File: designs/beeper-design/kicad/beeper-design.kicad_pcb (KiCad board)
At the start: 4 copper layers, 27.5 x 19 mm, 104 parts

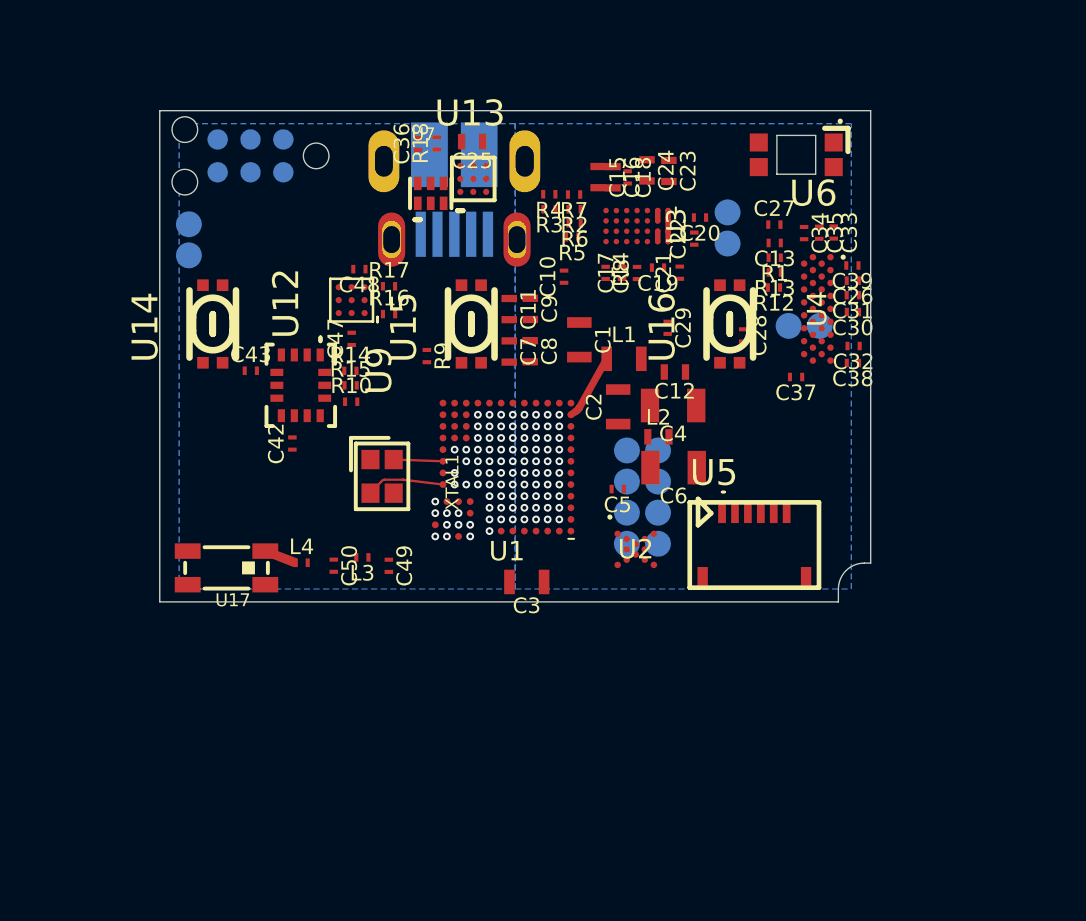
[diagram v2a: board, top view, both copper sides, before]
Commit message: better export + JLCPCB numbers
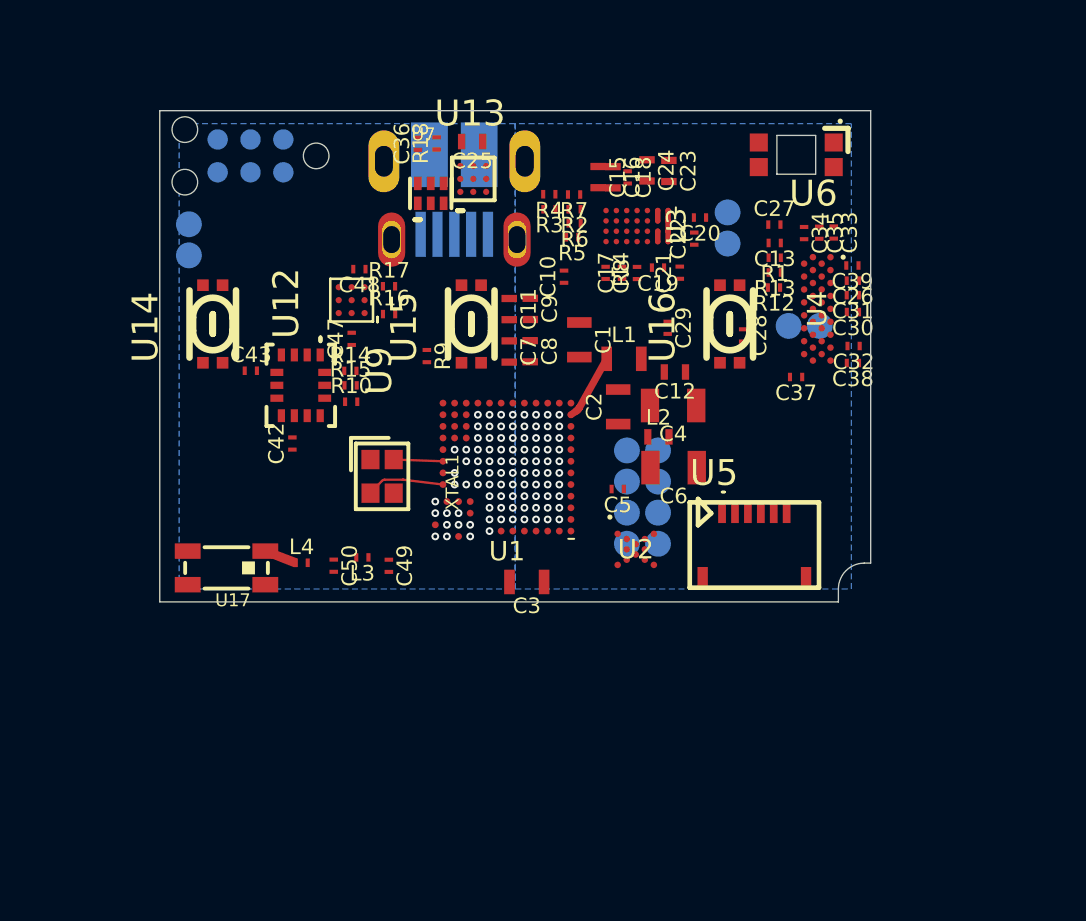
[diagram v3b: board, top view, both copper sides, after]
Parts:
- C10: footprint beeper-design:Pkg0201_18 -> beeper-design:Pkg0201_11
- C11: footprint beeper-design:Pkg0402_6 -> beeper-design:Pkg0402_1
- C12: footprint beeper-design:Pkg0402_5 -> beeper-design:Pkg0402
- C13: footprint beeper-design:Pkg0201_34 -> beeper-design:Pkg0201_27
- C14: footprint beeper-design:Pkg0201_2 -> beeper-design:Pkg0201_41
- C15: footprint beeper-design:Pkg0402_10 -> beeper-design:Pkg0402_5
- C16: footprint beeper-design:Pkg0402_4 -> beeper-design:Pkg0402_10
- C17: footprint beeper-design:Pkg0201_21 -> beeper-design:Pkg0201_14
- C18: footprint beeper-design:Pkg0201_33 -> beeper-design:Pkg0201_26
- C19: footprint beeper-design:Pkg0201_43 -> beeper-design:Pkg0201_36
- C20: footprint beeper-design:Pkg0201_6 -> beeper-design:Pkg0201_45
- C21: footprint beeper-design:Pkg0201_19 -> beeper-design:Pkg0201_12
- C22: footprint beeper-design:Pkg0201_30 -> beeper-design:Pkg0201_23
- C23: footprint beeper-design:Pkg0402_8 -> beeper-design:Pkg0402_3
- C24: footprint beeper-design:Pkg0402_2 -> beeper-design:Pkg0402_8
- C25: footprint beeper-design:Pkg0402 -> beeper-design:Pkg0402_6
- C26: footprint beeper-design:Pkg0201_44 -> beeper-design:Pkg0201_37
- C27: footprint beeper-design:Pkg0201_5 -> beeper-design:Pkg0201_44
- C28: footprint beeper-design:Pkg0201_17 -> beeper-design:Pkg0201_10
- C29: footprint beeper-design:Pkg0201_29 -> beeper-design:Pkg0201_22
- C30: footprint beeper-design:Pkg0201_15 -> beeper-design:Pkg0201_8
- C31: footprint beeper-design:Pkg0201_28 -> beeper-design:Pkg0201_21
- C32: footprint beeper-design:Pkg0201_40 -> beeper-design:Pkg0201_33
- C33: footprint beeper-design:Pkg0201_3 -> beeper-design:Pkg0201_42
- C34: footprint beeper-design:Pkg0201_14 -> beeper-design:Pkg0201_7
- C35: footprint beeper-design:Pkg0201_38 -> beeper-design:Pkg0201_31
- C36: footprint beeper-design:Pkg0201_31 -> beeper-design:Pkg0201_24
- C37: footprint beeper-design:Pkg0201_42 -> beeper-design:Pkg0201_35
- C38: footprint beeper-design:Pkg0201_4 -> beeper-design:Pkg0201_43
- C39: footprint beeper-design:Pkg0201_26 -> beeper-design:Pkg0201_19
- C42: footprint beeper-design:Pkg0201_45 -> beeper-design:Pkg0201_38
- C43: footprint beeper-design:Pkg0201_8 -> beeper-design:Pkg0201_1
- C47: footprint beeper-design:Pkg0201_10 -> beeper-design:Pkg0201_3
- C48: footprint beeper-design:Pkg0201_22 -> beeper-design:Pkg0201_15
- C49: footprint beeper-design:Pkg0201_39 -> beeper-design:Pkg0201_32
- C5: footprint beeper-design:Pkg0201_7 -> beeper-design:Pkg0201
- C50: footprint beeper-design:Pkg0201_9 -> beeper-design:Pkg0201_2
- C7: footprint beeper-design:Pkg0402_7 -> beeper-design:Pkg0402_2
- C8: footprint beeper-design:Pkg0402_9 -> beeper-design:Pkg0402_4
- C9: footprint beeper-design:Pkg0402_3 -> beeper-design:Pkg0402_9
- J1: value ~ -> TC2030-IDC-NL
- J6: value ~ -> 10103594-0001LF
- L2: footprint beeper-design:Pkg0402_1 -> beeper-design:Pkg0402_7
- L3: footprint beeper-design:Pkg0201_1 -> beeper-design:Pkg0201_40
- L4: footprint beeper-design:Pkg0201_16 -> beeper-design:Pkg0201_9
- R1: footprint beeper-design:Pkg0201_25 -> beeper-design:Pkg0201_18
- R10: footprint beeper-design:Pkg0201_41 -> beeper-design:Pkg0201_34
- R12, R13: footprint beeper-design:Pkg0201_27 -> beeper-design:Pkg0201_20
- R14, R15: footprint beeper-design:Pkg0201_12 -> beeper-design:Pkg0201_5
- R16, R17: footprint beeper-design:Pkg0201_37 -> beeper-design:Pkg0201_30
- R18: footprint beeper-design:Pkg0201_20 -> beeper-design:Pkg0201_13
- R2: footprint beeper-design:Pkg0201_13 -> beeper-design:Pkg0201_6
- R3: footprint beeper-design:Pkg0201_24 -> beeper-design:Pkg0201_17
- R4: footprint beeper-design:Pkg0201_36 -> beeper-design:Pkg0201_29
- R5: footprint beeper-design:Pkg0201 -> beeper-design:Pkg0201_39
- R6: footprint beeper-design:Pkg0201_11 -> beeper-design:Pkg0201_4
- R7: footprint beeper-design:Pkg0201_23 -> beeper-design:Pkg0201_16
- R8: footprint beeper-design:Pkg0201_35 -> beeper-design:Pkg0201_28
- R9: footprint beeper-design:Pkg0201_32 -> beeper-design:Pkg0201_25
- U1: value ~ -> DA14705-00000HZ2; footprint beeper-design:LP_1 -> beeper-design:LP
- U12: value ~ -> DRV2605YZFR; footprint beeper-design:LP -> beeper-design:LP_8
- U13: value ~ -> CSD75207W15; footprint beeper-design:LP_7 -> beeper-design:LP_6
- U14, U15, U16: value ~ -> EVPBB4A9B000; footprint beeper-design:LP_3 -> beeper-design:LP_2
- U2: value ~ -> AT25FF321A-UUN-T
- U3: value ~ -> BQ51003YFPR; footprint beeper-design:LP_8 -> beeper-design:LP_7
- U4: value ~ -> DA7212-01UM2; footprint beeper-design:LP_4 -> beeper-design:LP_3
- U5: value ~ -> FH19C-6S-0.5SH(10); footprint beeper-design:LP_6 -> beeper-design:LP_5
- U6: value ~ -> 23-23B/R6GHBHW-C30/2A; footprint beeper-design:LP_5 -> beeper-design:LP_4
- U7: value ~ -> TPD4S012DRYR
- U9: value ~ -> LSM6DSOXTR; footprint beeper-design:LP_2 -> beeper-design:LP_1
- XTAL1: value ~ -> XRCGB32M000F1H00R0
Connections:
- net AC1 renamed Net-(C15-Pad1)
- net AC2 renamed Net-(C16-Pad1)
- net AD renamed Net-(U3-AD)
- net BOOT1 renamed Net-(U3-BOOT1)
- net BOOT2 renamed Net-(U3-BOOT2)
- net CLAMP1 renamed Net-(U3-CLAMP1)
- net CLAMP2 renamed Net-(U3-CLAMP2)
- net COMM1 renamed Net-(U3-COMM1)
- net COMM2 renamed Net-(U3-COMM2)
- net D+ renamed /wpwr.module/D+
- net D- renamed /wpwr.module/D-
- net DACREF renamed Net-(U4-DACREF)
- net FOD renamed Net-(U3-FOD)
- net HPCFN renamed Net-(U4-HPCFN)
- net HPCFP renamed Net-(U4-HPCFP)
- net HPCSN renamed Net-(U4-HPCSN)
- net HPCSP renamed Net-(U4-HPCSP)
- net ILIM renamed Net-(U3-ILIM)
- net LX renamed Net-(U1H-LX)
- net LY renamed Net-(U1H-LY)
- net LZ renamed Net-(U1H-LZ)
- net MICBIAS1 renamed /board-io flex-conn.beeper-connector haptic.board-io.hapdrv.rs.collector/MICBIAS1
- net MICBIAS2 renamed Net-(U4-MICBIAS2)
- net OUT+ renamed Net-(U12-OUT+)
- net OUT- renamed Net-(U12-OUT-)
- net RECT renamed Net-(C23-Pad2)
- net REG renamed Net-(U12-REG)
- net RF1 renamed /wpwr.module/RF1
- net RF2 renamed /wpwr.module/RF2
- net RF3 renamed /wpwr.module/RF3
- net SP_N renamed /board-io flex-conn.beeper-connector haptic.board-io.hapdrv.rs.collector/SP_N
- net SP_P renamed /board-io flex-conn.beeper-connector haptic.board-io.hapdrv.rs.collector/SP_P
- net V12 renamed /wpwr.module/V12
- net V14RF renamed /wpwr.module/V14
- net V18F renamed /wpwr.module/V18F
- net V18P renamed /wpwr.module/V18P
- net VBAT renamed /wpwr.module/VBAT
- net VDD_A renamed Net-(U4-VDD_A)
- net VDIG renamed Net-(U4-VDIG)
- net VMID renamed Net-(U4-VMID)
- net VREF renamed Net-(U4-VREF)
- net XTAL32Mm renamed Net-(U1B-XTAL32Mm)
- net XTAL32Mp renamed Net-(U1B-XTAL32Mp)
- net board-io_codec-pdm_clk renamed /board-io flex-conn.beeper-connector haptic.board-io.hapdrv.rs.collector/board-io_codec-pdm_clk
- net board-io_codec-pdm_data renamed /board-io flex-conn.beeper-connector haptic.board-io.hapdrv.rs.collector/board-io_codec-pdm_data
- net board-io_qsen-i3c_scl renamed mcu_q-i3c_scl
- net cap_p1 renamed Net-(C22-Pad1)
- net mcu_VBUS renamed /wpwr.module/mcu_VBUS
- net mcu_dbg-m33_swdclk renamed /wpwr.module/mcu_mcu-dbg-m33_swdclk
- net mcu_dbg-m33_swdio renamed /wpwr.module/mcu_mcu-dbg-m33_swdio
- net mcu_mcu-etm_clk renamed /wpwr.module/mcu_mcu-etm_clk
- net mcu_mcu-etm_data0 renamed /wpwr.module/mcu_mcu-etm_data0
- net mcu_mcu-etm_data1 renamed /wpwr.module/mcu_mcu-etm_data1
- net mcu_mcu-etm_data2 renamed /wpwr.module/mcu_mcu-etm_data2
- net mcu_mcu-etm_data3 renamed /wpwr.module/mcu_mcu-etm_data3
- net mcu_mcu-mem_cs renamed /wpwr.module/mcu_mcu-mem_cs
- net mcu_mcu-mem_sck renamed /wpwr.module/mcu_mcu-mem_sck
- net mcu_mcu-mem_sdio0 renamed /wpwr.module/mcu_mcu-mem_sdio0
- net mcu_mcu-mem_sdio1 renamed /wpwr.module/mcu_mcu-mem_sdio1
- net mcu_mcu-mem_sdio2 renamed /wpwr.module/mcu_mcu-mem_sdio2
- net mcu_mcu-mem_sdio3 renamed /wpwr.module/mcu_mcu-mem_sdio3
- net nAD-EN renamed Net-(U13-D12)
- net rid_p1 renamed Net-(C36-Pad1)
- J1 pad 3: mcu_conn-uart_rx -> /wpwr.module/mcu_conn-uart_rx
- J1 pad 6: mcu_conn-uart_tx -> /wpwr.module/mcu_conn-uart_tx
- J6 pad 4: ID -> unconnected-(J6-ID-Pad4)
- U1 pad A1: (no net) -> unconnected-(U1A-OQSIF_D0-PadA1)
- U1 pad A2: (no net) -> unconnected-(U1A-OQSIF_D1-PadA2)
- U1 pad A3: (no net) -> unconnected-(U1A-OQSIF_D2-PadA3)
- U1 pad A4: mcu_q-spi_cs -> mcu_mcu-button2_gpio
- U1 pad A5: mcu_hap-i2c_sda -> mcu_mcu-wpwr2_gpio
- U1 pad A6: (no net) -> unconnected-(U1A-OQSIF_CS-PadA6)
- U1 pad B1: (no net) -> mcu_mcu-button1_gpio
- U1 pad B10: (no net) -> unconnected-(U1B-nRST-PadB10)
- U1 pad B11: (no net) -> unconnected-(U1D-P0_18-PadB11)
- U1 pad B12: mcu_q-spi_sck -> unconnected-(U1D-P0_06-PadB12)
- U1 pad B2: (no net) -> mcu_mcu-wpwr1_gpio
- U1 pad B3: (no net) -> unconnected-(U1A-OQSIF_D3-PadB3)
- U1 pad B4: (no net) -> unconnected-(U1A-OQSIF_CLK-PadB4)
- U1 pad B5: (no net) -> unconnected-(U1E-P1_16-PadB5)
- U1 pad B6: mcu_mcu-wpwr1_gpio -> unconnected-(U1D-P0_07-PadB6)
- U1 pad B7: mcu_hap-gpio1_gpio -> mcu_q-spi_sdo
- U1 pad B8: (no net) -> unconnected-(U1E-P1_04-PadB8)
- U1 pad C10: (no net) -> mcu_q-spi_sck
- U1 pad C11: (no net) -> mcu_mcu-wpwr0_gpio
- U1 pad C3: (no net) -> unconnected-(U1D-P0_25-PadC3)
- U1 pad C4: (no net) -> unconnected-(U1D-P0_26-PadC4)
- U1 pad C5: (no net) -> mcu_hap-i2c_scl
- U1 pad C6: (no net) -> unconnected-(U1E-P1_08-PadC6)
- U1 pad C8: (no net) -> unconnected-(U1D-P0_20-PadC8)
- U1 pad C9: (no net) -> unconnected-(U1E-P1_03-PadC9)
- U1 pad D1: (no net) -> unconnected-(U1E-P1_29-PadD1)
- U1 pad D10: (no net) -> unconnected-(U1D-P0_19-PadD10)
- U1 pad D11: (no net) -> unconnected-(U1D-P0_28-PadD11)
- U1 pad D2: mcu_q-spi_sdo -> mcu_c-i2c_sda
- U1 pad D3: mcu_c-i2c_sda -> mcu_hap-gpio0_gpio
- U1 pad D4: (no net) -> unconnected-(U1D-P0_12-PadD4)
- U1 pad D5: (no net) -> unconnected-(U1E-P1_02-PadD5)
- U1 pad D7: mcu_mcu-wpwr2_gpio -> unconnected-(U1D-P0_03-PadD7)
- U1 pad D8: mcu_mcu-button2_gpio -> unconnected-(U1D-P0_02-PadD8)
- U1 pad D9: mcu_hap-gpio0_gpio -> unconnected-(U1D-P0_05-PadD9)
- U1 pad E1: (no net) -> unconnected-(U1D-P0_13-PadE1)
- U1 pad E10: (no net) -> unconnected-(U1D-P0_21-PadE10)
- U1 pad E2: mcu_c-i2c_scl -> mcu_q-spi_cs
- U1 pad E3: (no net) -> mcu_c-i2c_scl
- U1 pad E4: (no net) -> /wpwr.module/mcu_conn-uart_rx
- U1 pad E5: (no net) -> unconnected-(U1E-P1_10-PadE5)
- U1 pad E6: (no net) -> /wpwr.module/mcu_conn-uart_tx
- U1 pad E7: mcu_q-spi_sdi -> unconnected-(U1D-P0_09-PadE7)
- U1 pad E8: (no net) -> unconnected-(U1E-P1_01-PadE8)
- U1 pad E9: mcu_mcu-wpwr3_gpio -> mcu_hap-i2c_sda
- U1 pad F2: (no net) -> unconnected-(U1E-P1_28-PadF2)
- U1 pad F3: mcu_mcu-button0_gpio -> unconnected-(U1E-P1_20-PadF3)
- U1 pad F4: (no net) -> unconnected-(U1E-P1_19-PadF4)
- U1 pad F7: (no net) -> unconnected-(U1D-P0_24-PadF7)
- U1 pad F8: mcu_mcu-button1_gpio -> unconnected-(U1D-P0_15-PadF8)
- U1 pad F9: (no net) -> unconnected-(U1D-P0_17-PadF9)
- U1 pad G10: mcu_mcu-wpwr0_gpio -> unconnected-(U1D-P0_08-PadG10)
- U1 pad G2: (no net) -> mcu_q-spi_sdi
- U1 pad G8: (no net) -> unconnected-(U1D-P0_16-PadG8)
- U1 pad G9: (no net) -> unconnected-(U1D-P0_10-PadG9)
- U1 pad H10: (no net) -> unconnected-(U1D-P0_30-PadH10)
- U1 pad H11: mcu_hap-i2c_scl -> mcu_hap-gpio1_gpio
- U1 pad H12: mcu_conn-uart_rx -> mcu_mcu-wpwr3_gpio
- U1 pad H2: (no net) -> unconnected-(U1D-P0_22-PadH2)
- U1 pad H4: (no net) -> unconnected-(U1E-P1_13-PadH4)
- U1 pad H9: (no net) -> unconnected-(U1D-P0_23-PadH9)
- U1 pad J10: (no net) -> unconnected-(U1C-NC-PadJ10)
- U1 pad J11: (no net) -> unconnected-(U1C-NC-PadJ11)
- U1 pad J12: (no net) -> unconnected-(U1C-NC-PadJ12)
- U1 pad J3: (no net) -> unconnected-(U1E-P1_24-PadJ3)
- U1 pad J6: (no net) -> unconnected-(U1E-P1_15-PadJ6)
- U1 pad J9: mcu_conn-uart_tx -> mcu_mcu-button0_gpio
- U1 pad K10: (no net) -> unconnected-(U1C-NC-PadK10)
- U1 pad K11: (no net) -> unconnected-(U1C-NC-PadK11)
- U1 pad K12: (no net) -> unconnected-(U1C-NC-PadK12)
- U1 pad K3: (no net) -> unconnected-(U1E-P1_07-PadK3)
- U1 pad K4: (no net) -> unconnected-(U1E-P1_00-PadK4)
- U1 pad L10: (no net) -> unconnected-(U1C-NC-PadL10)
- U1 pad L11: (no net) -> unconnected-(U1C-NC-PadL11)
- U1 pad L12: (no net) -> unconnected-(U1C-NC-PadL12)
- U1 pad L7: (no net) -> unconnected-(U1D-P0_27-PadL7)
- U1 pad M10: (no net) -> unconnected-(U1C-NC-PadM10)
- U1 pad M11: (no net) -> unconnected-(U1C-NC-PadM11)
- U1 pad M12: (no net) -> unconnected-(U1C-NC-PadM12)
- U1 pad M7: (no net) -> unconnected-(U1E-P1_05-PadM7)
- U1 pad M8: (no net) -> unconnected-(U1E-P1_06-PadM8)
- U1 pad M9: (no net) -> unconnected-(U1B-VAD-PadM9)
- U13 pad C1: (no net) -> unconnected-(U13-G2-PadC1)
- U2 pad A1: (no net) -> unconnected-(U2-NC-PadA1)
- U2 pad A5: (no net) -> unconnected-(U2-NC-PadA5)
- U2 pad G1: (no net) -> unconnected-(U2-NC-PadG1)
- U2 pad G5: (no net) -> unconnected-(U2-NC-PadG5)
- U4 pad A3: (no net) -> unconnected-(U4-HP_L-PadA3)
- U4 pad A5: (no net) -> unconnected-(U4-HP_R-PadA5)
- U4 pad B4: (no net) -> unconnected-(U4-GND_SENSE-PadB4)
- U4 pad C11: MCLK -> unconnected-(U4-MCLK-PadC11)
- U4 pad C13: (no net) -> unconnected-(U4-AUX_L-PadC13)
- U4 pad C15: (no net) -> unconnected-(U4-MIC2_N-PadC15)
- U4 pad C5: DATIN -> unconnected-(U4-DATIN-PadC5)
- U4 pad C7: DATOUT -> unconnected-(U4-DATOUT-PadC7)
- U4 pad D14: (no net) -> unconnected-(U4-AUX_R-PadD14)
- U4 pad D16: (no net) -> unconnected-(U4-MIC2_P-PadD16)
- U4 pad D4: BCLK -> unconnected-(U4-BCLK-PadD4)
- U4 pad D6: WCLK -> unconnected-(U4-WCLK-PadD6)
- U7 pad 3: (no net) -> unconnected-(U7-ID-Pad3)
- U7 pad 5: (no net) -> unconnected-(U7-NC-Pad5)
- U9 pad 10: (no net) -> unconnected-(U9-INT2-Pad10)
- U9 pad 11: imu_WCLK -> unconnected-(U9-WCLK-Pad11)
- U9 pad 2: TDMOUT -> unconnected-(U9-TDMOUT-Pad2)
- U9 pad 3: imu_BCLK -> unconnected-(U9-BCLK-Pad3)
- U9 pad 4: (no net) -> unconnected-(U9-INT1-Pad4)
- U9 pad 6: QVAR1 -> unconnected-(U9-AH1_QVAR1-Pad6)
- U9 pad 9: QVAR2 -> unconnected-(U9-AH2_QVAR2-Pad9)
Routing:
- net unconnected-(U1E-P1_28-PadF2): vias 0 -> 1
- net unconnected-(U1E-P1_24-PadJ3): vias 0 -> 1
- net unconnected-(U1E-P1_20-PadF3): vias 0 -> 1
- net unconnected-(U1E-P1_19-PadF4): vias 0 -> 1
- net unconnected-(U1E-P1_16-PadB5): vias 0 -> 1
- net unconnected-(U1E-P1_15-PadJ6): vias 0 -> 1
- net unconnected-(U1E-P1_13-PadH4): vias 0 -> 1
- net unconnected-(U1E-P1_10-PadE5): vias 0 -> 1
- net unconnected-(U1E-P1_08-PadC6): vias 0 -> 1
- net unconnected-(U1E-P1_07-PadK3): vias 0 -> 1
- net unconnected-(U1E-P1_04-PadB8): vias 0 -> 1
- net unconnected-(U1E-P1_02-PadD5): vias 0 -> 1
- net unconnected-(U1E-P1_01-PadE8): vias 0 -> 1
- net unconnected-(U1E-P1_00-PadK4): vias 0 -> 1
- net unconnected-(U1D-P0_30-PadH10): vias 0 -> 1
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- added copper zone on B.Cu, net unconnected-(U9-AH1_QVAR1-Pad6)
- added copper zone on B.Cu, net unconnected-(U9-AH2_QVAR2-Pad9)
- removed copper zone on B.Cu, net QVAR1
- removed copper zone on B.Cu, net QVAR2
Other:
- net class Default removed
- net class RF removed

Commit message: post export, had to munge sch
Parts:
- removed the ? at (145.0, 103.4)
- removed C33: 1u, beeper-design:Pkg0201_42
- removed C34: 1u, beeper-design:Pkg0201_7
- removed C35: 1u, beeper-design:Pkg0201_31
- removed the L2 at (145.0, 111.1)
- removed the U15 at (137.8, 106.8)
- removed U6: 23-23B/R6GHBHW-C30/2A, beeper-design:LP_4
- added D1: ~, beeper-design:LP_5, F.Cu at (142.1, 103.0)
- added J6: ~, beeper-design:AMPHENOL_10103594_0001LF, B.Cu at (137.1, 100.5)
- C1: footprint beeper-design:Pkg0603 -> beeper-design:Pkg0603_2
- C10: footprint beeper-design:Pkg0201_11 -> beeper-design:Pkg0201_42
- C11: footprint beeper-design:Pkg0402_1 -> beeper-design:Pkg0402_8
- C13: footprint beeper-design:Pkg0201_27 -> beeper-design:Pkg0201_10
- C14: footprint beeper-design:Pkg0201_41 -> beeper-design:Pkg0201_25
- C15: footprint beeper-design:Pkg0402_5 -> beeper-design:Pkg0201_21
- C16: footprint beeper-design:Pkg0402_10 -> beeper-design:Pkg0201_31
- C17: footprint beeper-design:Pkg0201_14 -> beeper-design:Pkg0201_45
- C18: footprint beeper-design:Pkg0201_26 -> beeper-design:Pkg0201_9
- C19: footprint beeper-design:Pkg0201_36 -> beeper-design:Pkg0201_18
- C2: footprint beeper-design:Pkg0603_1 -> beeper-design:Pkg0603
- C20: footprint beeper-design:Pkg0201_45 -> beeper-design:Pkg0201_30
- C21: footprint beeper-design:Pkg0201_12 -> beeper-design:Pkg0201_43
- C22: footprint beeper-design:Pkg0201_23 -> beeper-design:Pkg0201_7
- C23: footprint beeper-design:Pkg0402_3 -> beeper-design:Pkg0402_2
- C24: footprint beeper-design:Pkg0402_8 -> beeper-design:Pkg0402_6
- C25: footprint beeper-design:Pkg0402_6 -> beeper-design:Pkg0402_4
- C26: footprint beeper-design:Pkg0201_37 -> beeper-design:Pkg0201_27
- C27: footprint beeper-design:Pkg0201_44 -> beeper-design:Pkg0201_38
- C28: footprint beeper-design:Pkg0201_10 -> beeper-design:Pkg0201_5
- C29: footprint beeper-design:Pkg0201_22 -> beeper-design:Pkg0201_15
- C3: footprint beeper-design:Pkg0603_2 -> beeper-design:Pkg0603_1
- C30: footprint beeper-design:Pkg0201_8 -> beeper-design:Pkg0201_3
- C31: footprint beeper-design:Pkg0201_21 -> beeper-design:Pkg0201_13
- C32: footprint beeper-design:Pkg0201_33 -> beeper-design:Pkg0201_23
- C36: footprint beeper-design:Pkg0201_24 -> beeper-design:Pkg0201_8
- C37: footprint beeper-design:Pkg0201_35 -> beeper-design:Pkg0201_26
- C38: footprint beeper-design:Pkg0201_43 -> beeper-design:Pkg0201_37
- C39: footprint beeper-design:Pkg0201_19 -> beeper-design:Pkg0201_35
- C4: footprint beeper-design:Pkg0805_1 -> beeper-design:Pkg0805
- C42: footprint beeper-design:Pkg0201_38 -> beeper-design:Pkg0201_29
- C43: footprint beeper-design:Pkg0201_1 -> beeper-design:Pkg0201_39
- C47: footprint beeper-design:Pkg0201_3 -> beeper-design:Pkg0201_40
- C48: footprint beeper-design:Pkg0201_15 -> beeper-design:Pkg0201_6
- C49: footprint beeper-design:Pkg0201_32 -> beeper-design:Pkg0201_16
- C5: footprint beeper-design:Pkg0201 -> beeper-design:Pkg0201_32
- C50: footprint beeper-design:Pkg0201_2 -> beeper-design:Pkg0201_33
- C6: footprint beeper-design:Pkg0805 -> beeper-design:Pkg0805_1
- C7: footprint beeper-design:Pkg0402_2 -> beeper-design:Pkg0402_1
- C8: footprint beeper-design:Pkg0402_4 -> beeper-design:Pkg0402_3
- C9: footprint beeper-design:Pkg0402_9 -> beeper-design:Pkg0402_7
- J1: value TC2030-IDC-NL -> ~
- L1: footprint beeper-design:Pkg0603_3 -> beeper-design:Pkg0201_14
- L2: renamed from ?; value (none) -> 1u; footprint beeper-design:dummy5 -> beeper-design:Pkg0402_5
- L3: footprint beeper-design:Pkg0201_40 -> beeper-design:Pkg0201_24
- L4: footprint beeper-design:Pkg0201_9 -> beeper-design:Pkg0201_41
- R1: footprint beeper-design:Pkg0201_18 -> beeper-design:Pkg0201_4
- R10: footprint beeper-design:Pkg0201_34 -> beeper-design:Pkg0201_28
- R12, R13: footprint beeper-design:Pkg0201_20 -> beeper-design:Pkg0201_17
- R14, R15: footprint beeper-design:Pkg0201_5 -> beeper-design:Pkg0201_1
- R16, R17: footprint beeper-design:Pkg0201_30 -> beeper-design:Pkg0201_20
- R18: footprint beeper-design:Pkg0201_13 -> beeper-design:Pkg0201_44
- R2: footprint beeper-design:Pkg0201_6 -> beeper-design:Pkg0201_36
- R3: footprint beeper-design:Pkg0201_17 -> beeper-design:Pkg0201_2
- R4: footprint beeper-design:Pkg0201_29 -> beeper-design:Pkg0201_12
- R5: footprint beeper-design:Pkg0201_39 -> beeper-design:Pkg0201_22
- R6: footprint beeper-design:Pkg0201_4 -> beeper-design:Pkg0201_34
- R7: footprint beeper-design:Pkg0201_16 -> beeper-design:Pkg0201
- R8: footprint beeper-design:Pkg0201_28 -> beeper-design:Pkg0201_11
- R9: footprint beeper-design:Pkg0201_25 -> beeper-design:Pkg0201_19
- U1: value DA14705-00000HZ2 -> ~
- U12: value DRV2605YZFR -> ~
- U13: value CSD75207W15 -> ~
- U14, U16: value EVPBB4A9B000 -> ~
- U15: renamed from J6; value 10103594-0001LF -> ~; footprint beeper-design:AMPHENOL_10103594_0001LF -> beeper-design:LP_2; moved to F.Cu
- U2: value AT25FF321A-UUN-T -> ~
- U3: value BQ51003YFPR -> ~
- U4: value DA7212-01UM2 -> ~
- U5: value FH19C-6S-0.5SH(10) -> ~; footprint beeper-design:LP_5 -> beeper-design:LP_4
- U7: value TPD4S012DRYR -> ~
- U9: value LSM6DSOXTR -> ~
- XTAL1: value XRCGB32M000F1H00R0 -> ~
- moved ? 18.4 mm to (132.0, 116.0)
- moved ? 18.2 mm to (132.9, 115.8)
- moved ? 17.0 mm to (134.3, 115.8)
- moved ? 15.6 mm to (135.9, 115.4)
- moved L2 15.2 mm to (144.9, 111.1), turned to 270 degrees
- moved ? 12.6 mm to (130.4, 115.8)
- moved C13 11.5 mm to (144.5, 113.9), turned to 90 degrees
- moved TP11 11.0 mm to (140.3, 104.9)
- moved TP12 11.0 mm to (141.5, 104.9)
- moved R1 10.3 mm to (143.5, 112.5), turned to 90 degrees
- moved TP5 10.1 mm to (136.5, 106.2), turned to 90 degrees
- moved TP10 9.94 mm to (138.9, 106.2), turned to 180 degrees
- moved TP6 9.87 mm to (137.7, 106.2), turned to 270 degrees
- moved TP9 8.43 mm to (136.5, 107.4), turned to 270 degrees
- moved TP8 8.26 mm to (138.9, 107.4), turned to 180 degrees
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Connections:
- net /board-io flex-conn.beeper-connector haptic.board-io.hapdrv.rs.collector/MICBIAS1 renamed MICBIAS1
- net /board-io flex-conn.beeper-connector haptic.board-io.hapdrv.rs.collector/SP_N renamed SP_N
- net /board-io flex-conn.beeper-connector haptic.board-io.hapdrv.rs.collector/SP_P renamed SP_P
- net /board-io flex-conn.beeper-connector haptic.board-io.hapdrv.rs.collector/board-io_codec-pdm_clk renamed codec-pdm-net_clk
- net /board-io flex-conn.beeper-connector haptic.board-io.hapdrv.rs.collector/board-io_codec-pdm_data renamed codec-pdm-net_data
- net /wpwr.module/RF1 renamed RF1
- net /wpwr.module/RF2 renamed RF2
- net /wpwr.module/RF3 renamed RF3
- net /wpwr.module/V12 renamed V12
- net /wpwr.module/V14 renamed V14
- net /wpwr.module/V18F renamed V18F
- net /wpwr.module/V18P renamed V18P
- net /wpwr.module/VBAT renamed VBAT
- net /wpwr.module/mcu_VBUS renamed mcu_VBUS
- net /wpwr.module/mcu_mcu-dbg-m33_swdclk renamed mcu_mcu-dbg-m33_swdclk
- net /wpwr.module/mcu_mcu-dbg-m33_swdio renamed mcu_dbg-m33_swdio
- net /wpwr.module/mcu_mcu-etm_clk renamed mcu_mcu-etm_clk
- net /wpwr.module/mcu_mcu-etm_data0 renamed mcu_mcu-etm_data0
- net /wpwr.module/mcu_mcu-etm_data1 renamed mcu_mcu-etm_data1
- net /wpwr.module/mcu_mcu-etm_data2 renamed mcu_mcu-etm_data2
- net /wpwr.module/mcu_mcu-etm_data3 renamed mcu_mcu-etm_data3
- net Net-(C15-Pad1) renamed AC1
- net Net-(C16-Pad1) renamed AC2
- net Net-(C22-Pad1) renamed cap_p1
- net Net-(C23-Pad2) renamed RECT
- net Net-(U12-OUT+) renamed OUT+
- net Net-(U12-OUT-) renamed OUT-
- net Net-(U12-REG) renamed REG
- net Net-(U13-D12) renamed nAD-EN
- net Net-(U1B-XTAL32Mm) renamed XTAL32Mm
- net Net-(U1B-XTAL32Mp) renamed XTAL32Mp
- net Net-(U1H-LX) renamed LX
- net Net-(U1H-LY) renamed LY
- net Net-(U3-AD) renamed AD
- net Net-(U3-BOOT1) renamed BOOT1
- net Net-(U3-BOOT2) renamed BOOT2
- net Net-(U3-CLAMP1) renamed CLAMP1
- net Net-(U3-CLAMP2) renamed CLAMP2
- net Net-(U3-COMM1) renamed COMM1
- net Net-(U3-COMM2) renamed COMM2
- net Net-(U3-FOD) renamed FOD
- net Net-(U3-ILIM) renamed ILIM
- net Net-(U4-DACREF) renamed DACREF
- net Net-(U4-MICBIAS2) renamed MICBIAS2
- net Net-(U4-VDD_A) renamed VDD_MIC
- net Net-(U4-VDIG) renamed VDIG
- net Net-(U4-VMID) renamed VMID
- net Net-(U4-VREF) renamed VREF
- net mcu_q-i3c_scl renamed board-io_qsen-i3c_scl
- C11 pad 2: VDDSYS -> VDD1P8
- C12 pad 2: VDDSYS -> VDD1P8
- C13 pad 2: VDDSYS -> VDD1P8
- C14 pad 2: VDDSYS -> VDD1P8
- C29 pad 2: VDDSYS -> VDD1P8
- C36 pad 1: Net-(C36-Pad1) -> cap_cap_p1
- C4 pad 2: VDDSYS -> VDD1P8
- C42 pad 2: VDDSYS -> VDD1P8
- C43 pad 2: VDDSYS -> VDD1P8
- C48 pad 2: VDDSYS -> VDD1P8
- J1 pad 1: VDDSYS -> VDD1P8
- J1 pad 3: /wpwr.module/mcu_conn-uart_rx -> mcu_conn-uart_rx
- J1 pad 6: /wpwr.module/mcu_conn-uart_tx -> mcu_mcu-uart_tx
- R12 pad 1: mcu_c-i2c_sda -> codec-i2c-net_sda
- R12 pad 2: VDDSYS -> VDD1P8
- R13 pad 1: mcu_c-i2c_scl -> codec-i2c-net_scl
- R13 pad 2: VDDSYS -> VDD1P8
- R14 pad 2: VDDSYS -> VDD1P8
- R15 pad 2: VDDSYS -> VDD1P8
- R16 pad 2: VDDSYS -> VDD1P8
- R17 pad 2: VDDSYS -> VDD1P8
- R18 pad 1: Net-(C36-Pad1) -> cap_cap_p1
- U1 pad A1: unconnected-(U1A-OQSIF_D0-PadA1) -> (no net)
- U1 pad A2: unconnected-(U1A-OQSIF_D1-PadA2) -> (no net)
- U1 pad A3: unconnected-(U1A-OQSIF_D2-PadA3) -> (no net)
- U1 pad A4: mcu_mcu-button2_gpio -> (no net)
- U1 pad A5: mcu_mcu-wpwr2_gpio -> (no net)
- U1 pad A6: unconnected-(U1A-OQSIF_CS-PadA6) -> (no net)
- U1 pad B1: mcu_mcu-button1_gpio -> codec-i2c-net_scl
- U1 pad B10: unconnected-(U1B-nRST-PadB10) -> (no net)
- U1 pad B11: unconnected-(U1D-P0_18-PadB11) -> (no net)
- U1 pad B12: unconnected-(U1D-P0_06-PadB12) -> (no net)
- U1 pad B2: mcu_mcu-wpwr1_gpio -> (no net)
- U1 pad B3: unconnected-(U1A-OQSIF_D3-PadB3) -> (no net)
- U1 pad B4: unconnected-(U1A-OQSIF_CLK-PadB4) -> (no net)
- U1 pad B5: unconnected-(U1E-P1_16-PadB5) -> (no net)
- U1 pad B6: unconnected-(U1D-P0_07-PadB6) -> (no net)
- U1 pad B7: mcu_q-spi_sdo -> (no net)
- U1 pad B8: unconnected-(U1E-P1_04-PadB8) -> (no net)
- U1 pad C10: mcu_q-spi_sck -> (no net)
- U1 pad C11: mcu_mcu-wpwr0_gpio -> (no net)
- U1 pad C3: unconnected-(U1D-P0_25-PadC3) -> (no net)
- U1 pad C4: unconnected-(U1D-P0_26-PadC4) -> (no net)
- U1 pad C5: mcu_hap-i2c_scl -> (no net)
- U1 pad C6: unconnected-(U1E-P1_08-PadC6) -> (no net)
- U1 pad C8: unconnected-(U1D-P0_20-PadC8) -> (no net)
- U1 pad C9: unconnected-(U1E-P1_03-PadC9) -> (no net)
- U1 pad D1: unconnected-(U1E-P1_29-PadD1) -> (no net)
- U1 pad D10: unconnected-(U1D-P0_19-PadD10) -> (no net)
- U1 pad D11: unconnected-(U1D-P0_28-PadD11) -> mcu_mcu-button0_gpio
- U1 pad D2: mcu_c-i2c_sda -> (no net)
- U1 pad D3: mcu_hap-gpio0_gpio -> (no net)
- U1 pad D4: unconnected-(U1D-P0_12-PadD4) -> (no net)
- U1 pad D5: unconnected-(U1E-P1_02-PadD5) -> (no net)
- U1 pad D7: unconnected-(U1D-P0_03-PadD7) -> (no net)
- U1 pad D8: unconnected-(U1D-P0_02-PadD8) -> (no net)
- U1 pad D9: unconnected-(U1D-P0_05-PadD9) -> (no net)
- U1 pad E1: unconnected-(U1D-P0_13-PadE1) -> (no net)
- U1 pad E10: unconnected-(U1D-P0_21-PadE10) -> (no net)
- U1 pad E2: mcu_q-spi_cs -> (no net)
- U1 pad E3: mcu_c-i2c_scl -> (no net)
- U1 pad E4: /wpwr.module/mcu_conn-uart_rx -> (no net)
- U1 pad E5: unconnected-(U1E-P1_10-PadE5) -> (no net)
- U1 pad E6: /wpwr.module/mcu_conn-uart_tx -> (no net)
- U1 pad E7: unconnected-(U1D-P0_09-PadE7) -> (no net)
- U1 pad E8: unconnected-(U1E-P1_01-PadE8) -> (no net)
- U1 pad E9: mcu_hap-i2c_sda -> (no net)
- U1 pad F1: /wpwr.module/D+ -> D+
- U1 pad F2: unconnected-(U1E-P1_28-PadF2) -> (no net)
- U1 pad F3: unconnected-(U1E-P1_20-PadF3) -> mcu_mcu-mem_sdio3
- U1 pad F4: unconnected-(U1E-P1_19-PadF4) -> mcu_mcu-mem_sck
- U1 pad F7: unconnected-(U1D-P0_24-PadF7) -> (no net)
- U1 pad F8: unconnected-(U1D-P0_15-PadF8) -> (no net)
- U1 pad F9: unconnected-(U1D-P0_17-PadF9) -> (no net)
- U1 pad G1: /wpwr.module/D- -> D-
- U1 pad G10: unconnected-(U1D-P0_08-PadG10) -> mcu_hap-i2c_scl
- U1 pad G2: mcu_q-spi_sdi -> mcu_mcu-mem_sdio1
- U1 pad G3: /wpwr.module/mcu_mcu-mem_sdio1 -> (no net)
- U1 pad G4: /wpwr.module/mcu_mcu-mem_sdio3 -> (no net)
- U1 pad G8: unconnected-(U1D-P0_16-PadG8) -> mcu_conn-uart_rx
- U1 pad G9: unconnected-(U1D-P0_10-PadG9) -> mcu_mcu-uart_tx
- U1 pad H10: unconnected-(U1D-P0_30-PadH10) -> mcu_q-spi_sdi
- U1 pad H11: mcu_hap-gpio1_gpio -> mcu_q-spi_cs
- U1 pad H12: mcu_mcu-wpwr3_gpio -> mcu_q-spi_sck
- U1 pad H2: unconnected-(U1D-P0_22-PadH2) -> codec-i2c-net_sda
- U1 pad H3: /wpwr.module/mcu_mcu-mem_sck -> mcu_mcu-button2_gpio
- U1 pad H4: unconnected-(U1E-P1_13-PadH4) -> mcu_mcu-mem_sdio2
- U1 pad H5: /wpwr.module/mcu_mcu-mem_sdio2 -> (no net)
- U1 pad H9: unconnected-(U1D-P0_23-PadH9) -> mcu_hap-gpio1_gpio
- U1 pad J1: Net-(U1H-LZ) -> LZ
- U1 pad J10: unconnected-(U1C-NC-PadJ10) -> (no net)
- U1 pad J11: unconnected-(U1C-NC-PadJ11) -> (no net)
- U1 pad J12: unconnected-(U1C-NC-PadJ12) -> (no net)
- U1 pad J3: unconnected-(U1E-P1_24-PadJ3) -> mcu_mcu-mem_cs
- U1 pad J4: /wpwr.module/mcu_mcu-mem_sdio0 -> mcu_mcu-wpwr0_gpio
- U1 pad J5: /wpwr.module/mcu_mcu-mem_cs -> mcu_mcu-wpwr3_gpio
- U1 pad J6: unconnected-(U1E-P1_15-PadJ6) -> mcu_mcu-mem_sdio0
- U1 pad J9: mcu_mcu-button0_gpio -> mcu_hap-gpio0_gpio
- U1 pad K10: unconnected-(U1C-NC-PadK10) -> (no net)
- U1 pad K11: unconnected-(U1C-NC-PadK11) -> (no net)
- U1 pad K12: unconnected-(U1C-NC-PadK12) -> (no net)
- U1 pad K2: VDDSYS -> VDD1P8
- U1 pad K3: unconnected-(U1E-P1_07-PadK3) -> mcu_mcu-wpwr2_gpio
- U1 pad K4: unconnected-(U1E-P1_00-PadK4) -> mcu_mcu-wpwr1_gpio
- U1 pad L10: unconnected-(U1C-NC-PadL10) -> (no net)
- U1 pad L11: unconnected-(U1C-NC-PadL11) -> (no net)
- U1 pad L12: unconnected-(U1C-NC-PadL12) -> (no net)
- U1 pad L7: unconnected-(U1D-P0_27-PadL7) -> mcu_q-spi_sdo
- U1 pad M10: unconnected-(U1C-NC-PadM10) -> (no net)
- U1 pad M11: unconnected-(U1C-NC-PadM11) -> (no net)
- U1 pad M12: unconnected-(U1C-NC-PadM12) -> (no net)
- U1 pad M3: VDDSYS -> VDD1P8
- U1 pad M7: unconnected-(U1E-P1_05-PadM7) -> mcu_hap-i2c_sda
- U1 pad M8: unconnected-(U1E-P1_06-PadM8) -> mcu_mcu-button1_gpio
- U1 pad M9: unconnected-(U1B-VAD-PadM9) -> (no net)
- U12 pad C2: VDDSYS -> VDD1P8
- U13 pad B2: VDDSYS -> VDD1P8
- U13 pad C1: unconnected-(U13-G2-PadC1) -> (no net)
- U13 pad C2: VDDSYS -> VDD1P8
- U13 pad C3: VDDSYS -> VDD1P8
- U2 pad A1: unconnected-(U2-NC-PadA1) -> (no net)
- U2 pad A5: unconnected-(U2-NC-PadA5) -> (no net)
- U2 pad B2: VDDSYS -> VDD1P8
- U2 pad B4: /wpwr.module/mcu_mcu-mem_cs -> mcu_mcu-mem_cs
- U2 pad D2: /wpwr.module/mcu_mcu-mem_sdio3 -> mcu_mcu-mem_sdio3
- U2 pad D4: /wpwr.module/mcu_mcu-mem_sdio1 -> mcu_mcu-mem_sdio1
- U2 pad E3: /wpwr.module/mcu_mcu-mem_sdio0 -> mcu_mcu-mem_sdio0
- U2 pad F2: /wpwr.module/mcu_mcu-mem_sck -> mcu_mcu-mem_sck
- U2 pad F4: /wpwr.module/mcu_mcu-mem_sdio2 -> mcu_mcu-mem_sdio2
- U2 pad G1: unconnected-(U2-NC-PadG1) -> (no net)
- U2 pad G5: unconnected-(U2-NC-PadG5) -> (no net)
- U3 pad D1: VDDSYS -> VDD1P8
- U3 pad D2: VDDSYS -> VDD1P8
- U3 pad D3: VDDSYS -> VDD1P8
- U3 pad D4: VDDSYS -> VDD1P8
- U4 pad A1: Net-(U4-HPCSP) -> (no net)
- U4 pad A11: VDDSYS -> VDD1P8
- U4 pad A3: unconnected-(U4-HP_L-PadA3) -> (no net)
- U4 pad A5: unconnected-(U4-HP_R-PadA5) -> (no net)
- U4 pad B4: unconnected-(U4-GND_SENSE-PadB4) -> (no net)
- U4 pad C1: Net-(U4-HPCSN) -> (no net)
- U4 pad C11: unconnected-(U4-MCLK-PadC11) -> MCLK
- U4 pad C13: unconnected-(U4-AUX_L-PadC13) -> (no net)
- U4 pad C15: unconnected-(U4-MIC2_N-PadC15) -> (no net)
- U4 pad C3: Net-(U4-HPCFN) -> (no net)
- U4 pad C5: unconnected-(U4-DATIN-PadC5) -> DATIN
- U4 pad C7: unconnected-(U4-DATOUT-PadC7) -> DATOUT
- U4 pad C9: mcu_c-i2c_sda -> codec-i2c-net_sda
- U4 pad D14: unconnected-(U4-AUX_R-PadD14) -> (no net)
- U4 pad D16: unconnected-(U4-MIC2_P-PadD16) -> (no net)
- U4 pad D2: Net-(U4-HPCFP) -> (no net)
- U4 pad D4: unconnected-(U4-BCLK-PadD4) -> BCLK
- U4 pad D6: unconnected-(U4-WCLK-PadD6) -> WCLK
- U4 pad D8: mcu_c-i2c_scl -> codec-i2c-net_scl
- U7 pad 1: /wpwr.module/D+ -> D+
- U7 pad 2: /wpwr.module/D- -> D-
- U7 pad 3: unconnected-(U7-ID-Pad3) -> (no net)
- U7 pad 5: unconnected-(U7-NC-Pad5) -> (no net)
- U9 pad 10: unconnected-(U9-INT2-Pad10) -> (no net)
- U9 pad 11: unconnected-(U9-WCLK-Pad11) -> imu_WCLK
- U9 pad 2: unconnected-(U9-TDMOUT-Pad2) -> TDMOUT
- U9 pad 3: unconnected-(U9-BCLK-Pad3) -> imu_BCLK
- U9 pad 4: unconnected-(U9-INT1-Pad4) -> (no net)
- U9 pad 5: VDDSYS -> VDD1P8
- U9 pad 6: unconnected-(U9-AH1_QVAR1-Pad6) -> QVAR1
- U9 pad 8: VDDSYS -> VDD1P8
- U9 pad 9: unconnected-(U9-AH2_QVAR2-Pad9) -> QVAR2
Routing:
- net VDD1P8: track 0.00 -> 29.5 mm, vias 0 -> 19
- net QVAR2: track 0.00 -> 23.1 mm, vias 0 -> 1
- net mcu_mcu-dbg-m33_swdclk: track 0.00 -> 22.6 mm
- net D-: track 0.00 -> 20.3 mm, vias 0 -> 2
- net mcu_dbg-m33_swdio: track 0.00 -> 18.3 mm, vias 1 -> 2
- net codec-i2c-net_scl: track 0.00 -> 18.0 mm, vias 0 -> 1
- net D+: track 0.00 -> 17.6 mm, vias 0 -> 2
- net mcu_mcu-wpwr3_gpio: track 0.00 -> 16.1 mm, vias 0 -> 2
- net mcu_mcu-wpwr1_gpio: track 0.00 -> 15.4 mm, vias 1 -> 2
- net mcu_conn-uart_rx: track 0.00 -> 15.2 mm, vias 0 -> 2
- net VLED: track 0.00 -> 14.3 mm
- net mcu_mcu-uart_tx: track 0.00 -> 14.1 mm, vias 0 -> 2
- net V14: track 0.00 -> 13.5 mm, vias 1 -> 2
- net mcu_mcu-etm_data2: track 0.00 -> 13.3 mm, vias 1 -> 3
- net codec-i2c-net_sda: track 0.00 -> 13.3 mm, vias 0 -> 2
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- added copper zone on F.Cu, net GND
- added copper zone on B.Cu, net QVAR1
- added copper zone on B.Cu, net QVAR2
- added copper zone on In2.Cu, net VDD1P8
- removed copper zone on In2.Cu, net VDDSYS
- removed copper zone on B.Cu, net unconnected-(U9-AH1_QVAR1-Pad6)
- removed copper zone on B.Cu, net unconnected-(U9-AH2_QVAR2-Pad9)
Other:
- outline, holes or cut-outs redrawn
- net class BGA added: clearance 0.065, trace_width 0.075, via_dia 0.015, via_drill 0.15
- net class Default added: clearance 0.0625, trace_width 0.075, via_dia 0.015, via_drill 0.15
- net class RF added: clearance 0.0625, trace_width 0.3493, via_dia 0.015, via_drill 0.15

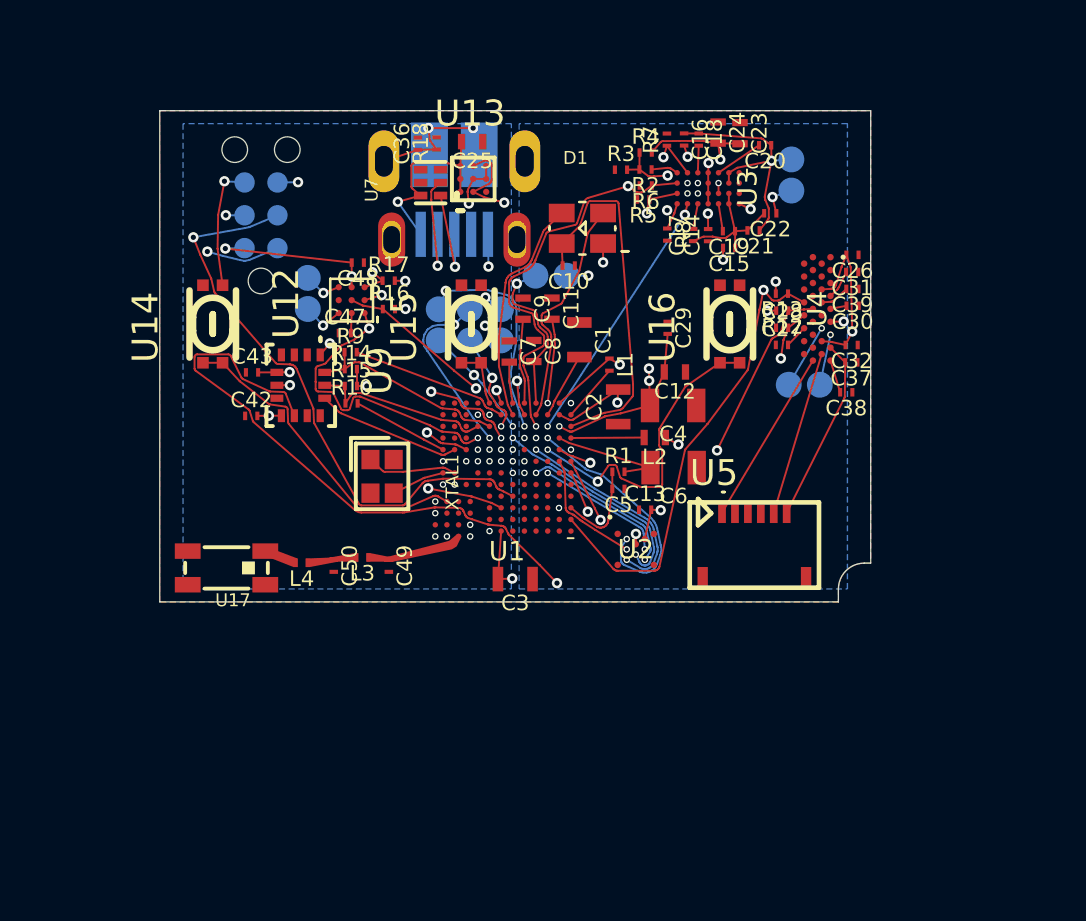
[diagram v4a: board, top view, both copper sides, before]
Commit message: fixing drc errors
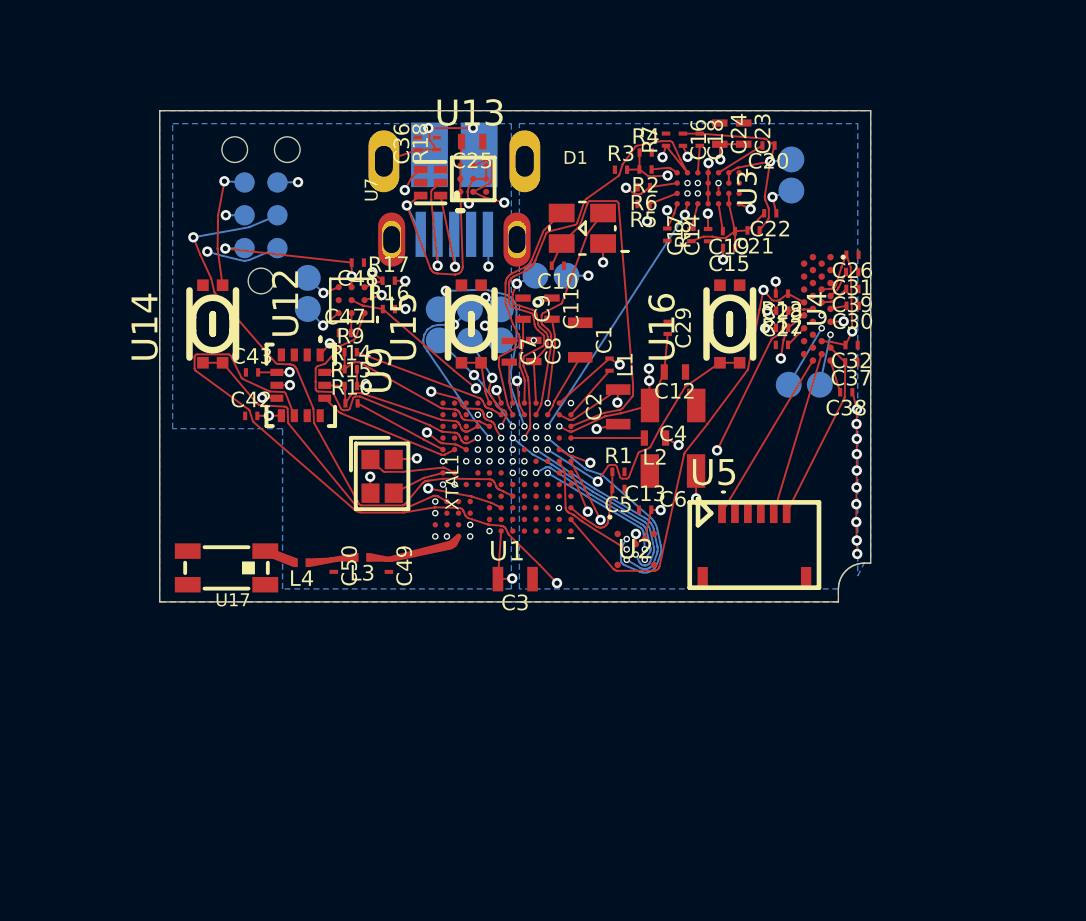
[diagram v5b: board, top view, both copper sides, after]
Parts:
- moved C10 0.42 mm to (141.1, 104.5)
- moved R5 0.18 mm to (144.5, 102.1)
- moved C23 0.14 mm to (148.3, 99.4)
- moved C6 0.13 mm to (145.6, 112.4)
- moved C20 0.13 mm to (149.3, 99.8)
- moved R6 0.10 mm to (144.5, 101.5)
- moved C24 0.08 mm to (147.4, 99.4)
- moved C17 0.07 mm to (146.3, 103.3)
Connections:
- U1 pad J4: mcu_mcu-wpwr0_gpio -> mcu_mcu-wpwr1_gpio
- U1 pad K4: mcu_mcu-wpwr1_gpio -> mcu_mcu-wpwr0_gpio
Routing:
- net GND: track 8.57 -> 20.9 mm, vias 29 -> 49
- net V18P: track 4.73 -> 0.00 mm
- net mcu_mcu-wpwr3_gpio: track 16.1 -> 19.6 mm
- net VBUS: track 7.67 -> 10.8 mm
- net RECT: track 5.57 -> 2.83 mm
- net mcu_mcu-wpwr0_gpio: track 13.3 -> 10.9 mm
- net mcu_mcu-wpwr1_gpio: track 15.4 -> 13.5 mm
- net mcu_mcu-button2_gpio: track 12.1 -> 10.8 mm
- net board-io_rgb_g: track 8.81 -> 9.36 mm
- net mcu_hap-gpio0_gpio: track 11.7 -> 11.4 mm, vias 2 -> 1
